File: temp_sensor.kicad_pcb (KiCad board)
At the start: 2 copper layers, 40 x 35 mm, 26 parts, among them J2 Conn_01x06, J3 Conn_01x08, J4 Conn_01x08, SW1 Boot, SW2 Reset, U1 HDC3020DEFR, U2 ESP-12F, U3 TPS613221ADBVR, U4 TLV74033PDBVR

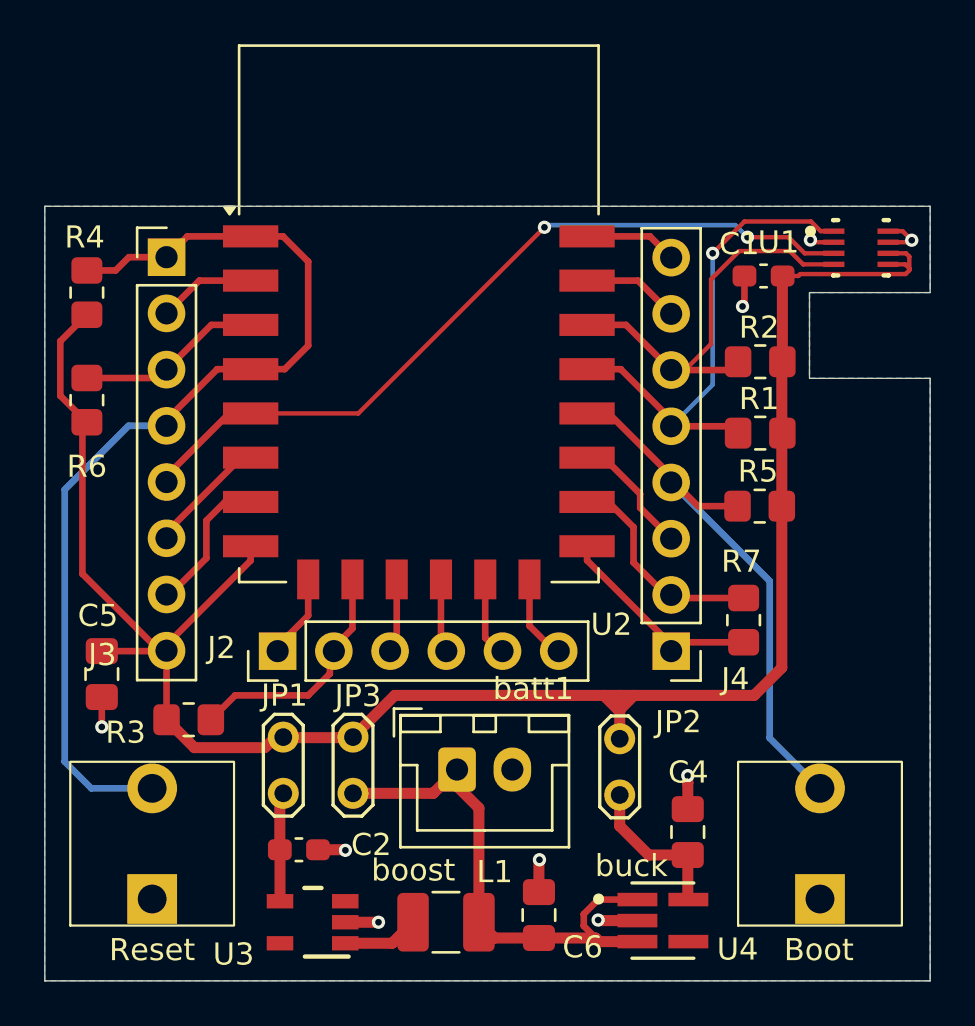
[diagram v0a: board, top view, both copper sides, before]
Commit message: Added cap at reset and screw hole
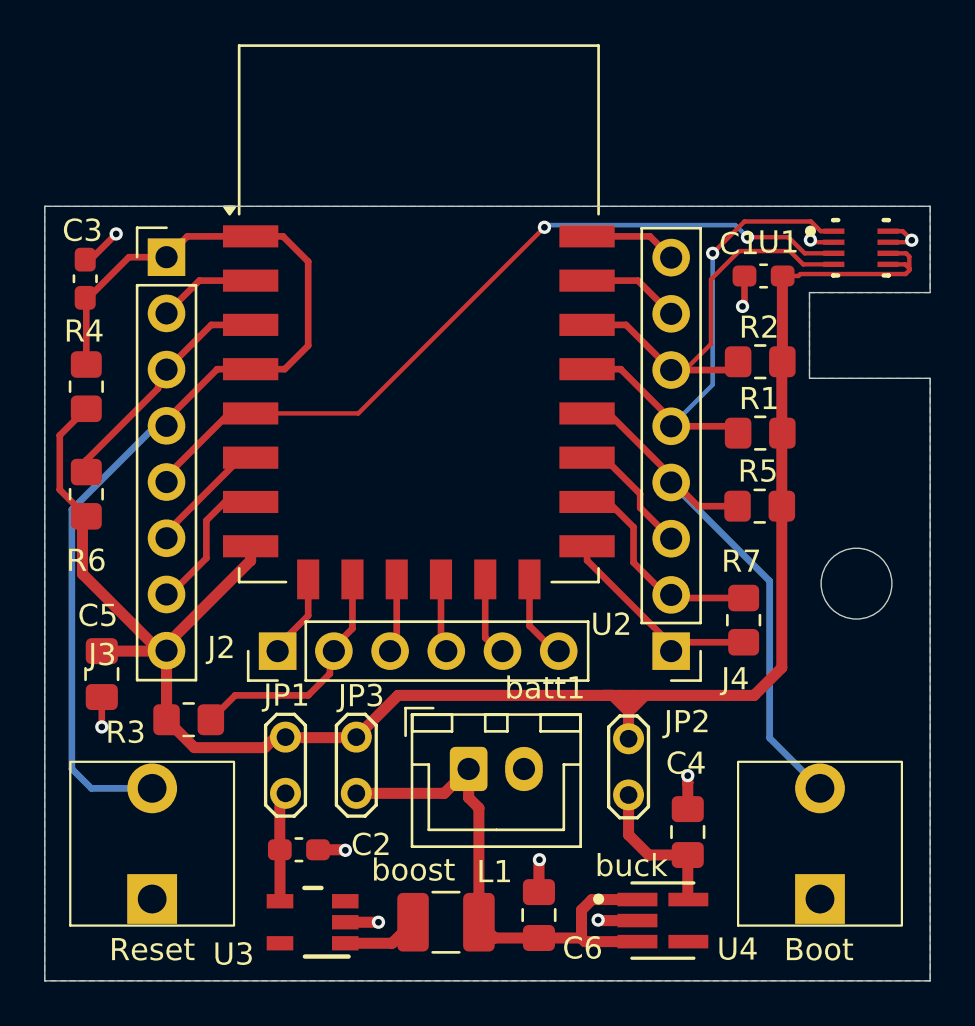
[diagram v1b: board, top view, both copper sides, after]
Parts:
- added C3: 10nF, Capacitor_SMD:C_0603_1608Metric_Pad1.08x0.95mm_HandSolder, F.Cu at (41.8, 43.3)
- added screw: MountingHole_3.2mm_M3_ISO7380, MountingHole:MountingHole_3.2mm_M3_ISO7380, F.Cu at (76.7, 57.0)
- moved R4 4.25 mm to (41.9, 48.1)
- moved R6 4.25 mm to (41.9, 53.0)
- moved batt1 0.53 mm to (59.1, 65.4)
- moved JP2 0.40 mm to (66.4, 66.6)
- moved JP3 0.15 mm to (54.1, 66.5)
- moved JP1 0.10 mm to (50.9, 66.5)
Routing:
- net +3V3: track 90.2 -> 86.5 mm
- net /wake: track 45.5 -> 48.0 mm
- net Net-(J3-Pin_3): track 8.39 -> 10.8 mm
- net GNDREF: track 23.1 -> 25.0 mm, vias 9 -> 10
